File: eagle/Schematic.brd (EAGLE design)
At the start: 37.8 x 16.5 mm, 28 parts, among them U1 ATMEGA328P, X1 12MHz, X2 16MHz

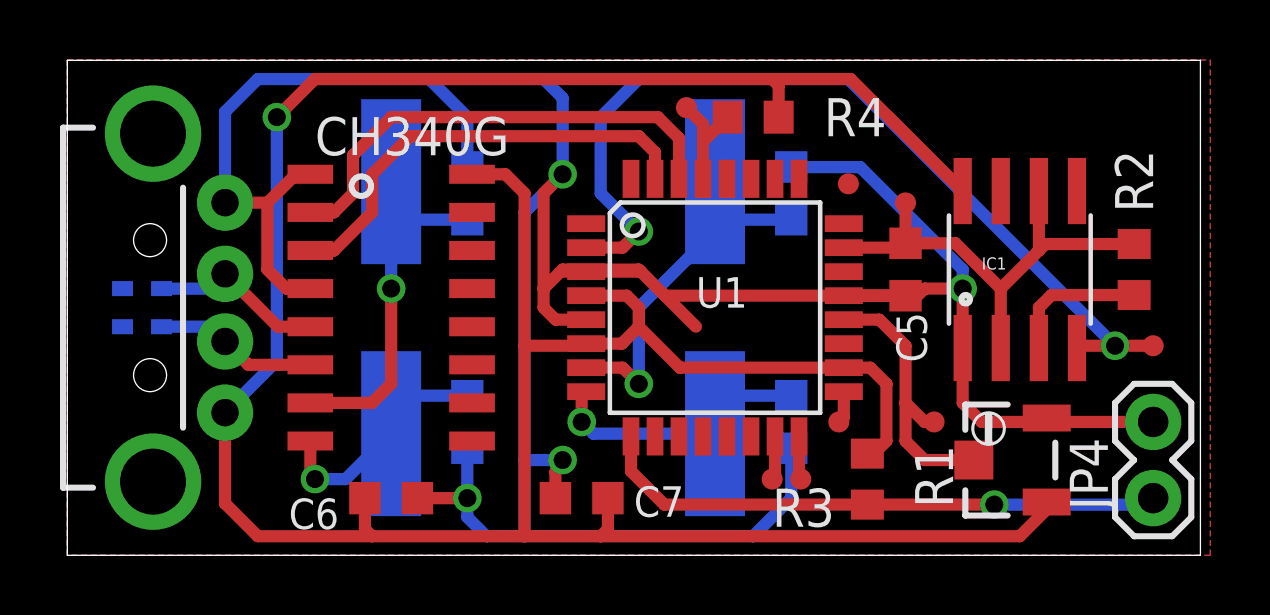
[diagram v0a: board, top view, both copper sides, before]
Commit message: Added DTR reset, converted XTAL to smaller ones.
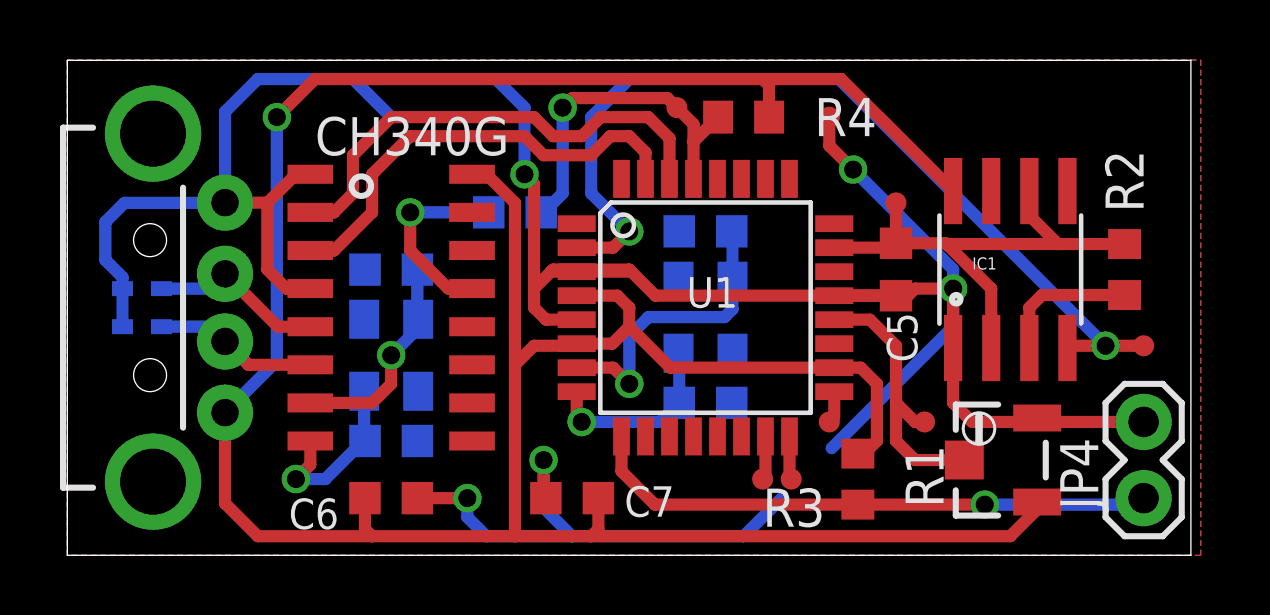
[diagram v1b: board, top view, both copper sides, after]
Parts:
- removed X1: 12MHz, IQD-Frequency-Products:HC49-4-HSMX
- removed X2: 16MHz, IQD-Frequency-Products:HC49-4-HSMX
- added C8: 100nF, rcl:C0603K
- added Q1: 16MHz, seb:MT
- added Q2: 12Mhz, seb:MT
- moved C3 3.59 mm to (10.8, 9.53), turned to 180 degrees
- moved C1 3.13 mm to (21.3, 10.8), turned to 180 degrees
- moved C2 2.93 mm to (21.3, 5.08), turned to 0 degrees
- moved C4 2.62 mm to (10.8, 3.81), turned to 0 degrees
- moved TP1 2.31 mm to (25.4, 14.6)
- moved C5 0.32 mm to (27.6, 9.53)
- moved JP4 0.32 mm to (35.9, 1.91)
- moved R1 0.32 mm to (31.1, 3.17)
- moved R2 0.32 mm to (35.2, 9.53)
- moved R3 0.32 mm to (26.4, 2.54)
- moved TP2 0.32 mm to (25.4, 4.45)
- moved TP3 0.32 mm to (24.1, 2.54)
- moved TP4 0.32 mm to (23.2, 2.54)
- moved TP6 0.32 mm to (35.9, 6.99)
- moved TP7 0.32 mm to (27.6, 11.7)
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- renumbered U$1 to U2
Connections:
- new net N$6: C8.1, U2.13
- net N$2: now also Q2.3; no longer X1.2
- net N$3: now also Q2.1; no longer X1.1
- net N$4: now also Q1.3; no longer X2.2
- net N$5: now also Q1.1; no longer X2.1
- net RST: now also C8.2
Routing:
- net RST: track 3.76 -> 11.7 mm, vias 0 -> 1
- net N$6: track 0.00 -> 6.58 mm, vias 0 -> 1
- net N$2: track 12.4 -> 7.15 mm
- net GND: track 106.0 -> 101.4 mm, vias 4 -> 5
- net N$5: track 8.97 -> 6.26 mm
- net N$4: track 12.4 -> 9.98 mm
- net N$3: track 7.79 -> 5.95 mm
- net AD0: track 16.3 -> 17.3 mm
- net VCC: track 106.8 -> 105.9 mm
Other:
- board size 37.8 x 16.5 mm -> 37.5 x 16.5 mm

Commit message: Fix PCB errors after first prototype.
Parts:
- added C9: 100nF, rcl:C0603K
- TP1, TP2, TP3, TP4, TP5, TP6, TP7, TP8: value TPTP07R -> TPTP10R; device testpad:TP07R -> testpad:TP10R
- moved TP4 1.27 mm to (24.4, 2.54)
- moved TP3 1.27 mm to (22.9, 2.54)
- moved TP1 0.64 mm to (26.0, 14.6)
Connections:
- new net N$7: C9.1, U2.4
- net GND: now also C9.2; no longer U2.4
- net MISO: now also U1.16; no longer U1.15
- net MOSI: now also U1.15; no longer U1.16
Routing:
- net VCC: track 105.9 -> 86.1 mm, vias 1 -> 2
- net N$7: track 0.00 -> 12.1 mm, vias 0 -> 1
- net GND: track 101.4 -> 107.9 mm, vias 5 -> 6
- net N$6: track 6.58 -> 7.93 mm
